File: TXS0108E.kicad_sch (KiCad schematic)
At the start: 1 part, among them U6 MAX98357A

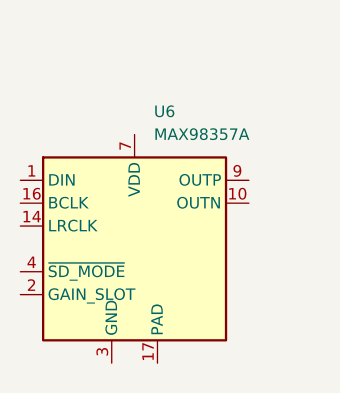
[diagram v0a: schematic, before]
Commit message: Add components: TXS0108E, FT232 oscillators/power/USB, symbol library table
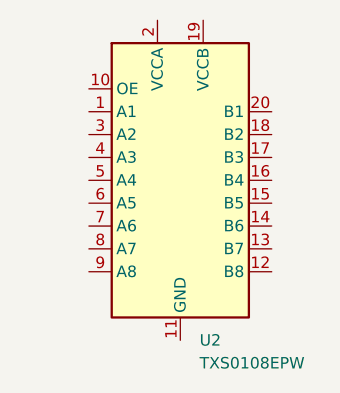
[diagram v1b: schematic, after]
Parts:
- removed U6: MAX98357A, Package_DFN_QFN:TQFN-16-1EP_3x3mm_P0.5mm_EP1.23x1.23mm, symbol Audio:MAX98357A
- added U2: TXS0108EPW, Package_SO:TSSOP-20_4.4x6.5mm_P0.65mm, symbol Logic_LevelTranslator:TXS0108EPW
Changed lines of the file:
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@@
 	(paper "A4")
 	(symbol
-		(lib_id "Audio:MAX98357A")
-		(at 144.78 99.06 0)
+		(lib_id "Logic_LevelTranslator:TXS0108EPW")
+		(at 149.86 91.44 0)
 		(unit 1)
 		(body_style 1)
@@
 		(dnp no)
 		(fields_autoplaced yes)
-		(property "Reference" "U6"
-			(at 146.9233 83.82 0)
+		(property "Reference" "U2"
+			(at 152.0033 109.22 0)
 			(show_name no)
 			(do_not_autoplace no)
@@
 			)
 		)
-		(property "Value" "MAX98357A"
-			(at 146.9233 86.36 0)
+		(property "Value" "TXS0108EPW"
+			(at 152.0033 111.76 0)
 			(show_name no)
 			(do_not_autoplace no)
@@
 			)
 		)
-		(property "Footprint" "Package_DFN_QFN:TQFN-16-1EP_3x3mm_P0.5mm_EP1.23x1.23mm"
-			(at 143.51 101.6 0)
+		(property "Footprint" "Package_SO:TSSOP-20_4.4x6.5mm_P0.65mm"
+			(at 149.86 110.49 0)
 			(hide yes)
 			(show_name no)
@@
 			)
 		)
-		(property "Datasheet" "https://www.analog.com/media/en/technical-documentation/data-sheets/MAX98357A-MAX98357B.pdf"
-			(at 144.78 101.6 0)
+		(property "Datasheet" "www.ti.com/lit/ds/symlink/txs0108e.pdf"
+			(at 149.86 93.98 0)
 			(hide yes)
 			(show_name no)
@@
 			)
 		)
-		(property "Description" "Mono DAC with amplifier, I2S, PCM, TDM, 32-bit, 96khz, 3.2W, TQFP-16"
-			(at 144.78 99.06 0)
+		(property "Description" "Bidirectional  level-shifting voltage translator, TSSOP-20"
+			(at 149.86 91.44 0)
 			(hide yes)
 			(show_name no)
@@
 			)
 		)
-		(pin "16"
+		(pin "19"
+		)
+		(pin "20"
+		)
+		(pin "14"
+		)
+		(pin "2"
+		)
+		(pin "5"
+		)
+		(pin "17"
+		)
+		(pin "7"
 		)
 		(pin "4"
 		)
-		(pin "5"
+		(pin "3"
 		)
-		(pin "15"
-		)
-		(pin "12"
-		)
-		(pin "13"
-		)
-		(pin "17"
-		)
-		(pin "2"
-		)
-		(pin "3"
+		(pin "18"
 		)
 		(pin "9"
 		)
-		(pin "1"
+		(pin "16"
 		)
 		(pin "10"
@@
 		(pin "11"
 		)
+		(pin "8"
+		)
+		(pin "12"
+		)
+		(pin "15"
+		)
+		(pin "13"
+		)
 		(pin "6"
 		)
-		(pin "7"
-		)
-		(pin "14"
-		)
-		(pin "8"
+		(pin "1"
 		)
 		(instances
 			(project "esp32_xiaozhi"
-				(path "/cae338e8-f342-43cb-b99a-a0486629133c/0b8c63fc-3109-4f1a-8140-b91a685f434f"
-					(reference "U6")
+				(path "/cae338e8-f342-43cb-b99a-a0486629133c/2567bb9e-06b8-4d2c-80a7-ee2453b67a65"
+					(reference "U2")
 					(unit 1)
 				)

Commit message: ESP32S3 branch initial changes
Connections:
- net A1: now reaches U2.1 (A1)
- net OE: now reaches U2.10 (OE)
- net GND: now reaches U2.11 (GND)
- net B8: now reaches U2.12 (B8)
- net B7: now reaches U2.13 (B7)
- net B6: now reaches U2.14 (B6)
- net B5: now reaches U2.15 (B5)
- net B4: now reaches U2.16 (B4)
- net B3: now reaches U2.17 (B3)
- net B2: now reaches U2.18 (B2)
- net +5V: now reaches U2.19 (VCCB)
- net +3V3: now reaches U2.2 (VCCA)
- net B1: now reaches U2.20 (B1)
- net A2: now reaches U2.3 (A2)
- net A3: now reaches U2.4 (A3)
- net A4: now reaches U2.5 (A4)
- net A5: now reaches U2.6 (A5)
- net A6: now reaches U2.7 (A6)
- net A7: now reaches U2.8 (A7)
- net A8: now reaches U2.9 (A8)

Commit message: Update KiCad project files
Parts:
- added C36, C37, C38: 100nf, Capacitor_SMD:C_0805_2012Metric, symbol Device:C
- added J11: Conn_01x08_Pin, symbol Connector:Conn_01x08_Pin
- added JP5, JP6: NL, Jumper:SolderJumper-2_P1.3mm_Open_RoundedPad1.0x1.5mm, symbol Jumper:Jumper_2_Open
- added Q10, Q11: FDN306P, Package_TO_SOT_SMD:SOT-23W, symbol FDN306P:FDN306P
- added Q7, Q8: Q_NPN_BCE, Package_TO_SOT_SMD:SOT-23W, symbol Device:Q_NPN_BCE
- added Q9: 2N7002, Package_TO_SOT_SMD:SOT-23, symbol Transistor_FET:2N7002
- added R49, R50, R51, R52, R53: 10k, Resistor_SMD:R_0603_1608Metric, symbol Device:R
- renumbered U2 to U7
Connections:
- net +3V3: now also C36.1, C37.1, JP5.2 (B), R50.2, R52.2
- net +5V: now also C38.1, JP6.2 (B)
- net B1: now also J11.1 (Pin_1)
- net B2: now also J11.2 (Pin_2)
- net B3: now also J11.3 (Pin_3)
- net B4: now also J11.4 (Pin_4)
- net B5: now also J11.5 (Pin_5)
- net B6: now also J11.6 (Pin_6)
- net B7: now also J11.7 (Pin_7)
- net B8: now also J11.8 (Pin_8)
- net GND: now also C36.2, C37.2, C38.2, Q7.3 (E), Q8.3 (E), Q9.2 (S), R53.1
- net OE: now also Q11.1, Q9.1 (G), R49.1, R53.2; no longer U7.10 (OE)
- new net: Q10.1, Q11.2, Q9.3 (D)
- new net: Q7.2 (C), R50.1, R51.1
- new net: Q8.1 (B), R51.2
- new net: JP5.1 (A), JP6.1 (A), Q10.3, Q11.3
- new net: Q7.1 (B), R49.2
- new net OEN: Q8.2 (C), R52.1, U7.10 (OE)
- new net vcc: Q10.2

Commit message: Remove unused schematic files, lock files, and backup directories
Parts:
- removed J11: Conn_01x08_Pin, symbol Connector:Conn_01x08_Pin
- added J11: logic_convert, Connector_PinHeader_1.27mm:PinHeader_1x09_P1.27mm_Vertical, symbol Connector:Conn_01x09_Pin
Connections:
- net B1: now also J11.1 (Pin_1)
- net B2: now also J11.2 (Pin_2)
- net B3: now also J11.3 (Pin_3)
- net B4: now also J11.4 (Pin_4)
- net B5: now also J11.5 (Pin_5)
- net B6: now also J11.6 (Pin_6)
- net B7: now also J11.7 (Pin_7)
- net B8: now also J11.8 (Pin_8)
- net GND: now also J11.9 (Pin_9)
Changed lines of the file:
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@@
+	(symbol
+		(lib_id "power:GND")
+		(at 191.77 104.14 0)
+		(unit 1)
+		(body_style 1)
+		(exclude_from_sim no)
+		(in_bom yes)
+		(on_board yes)
+		(in_pos_files yes)
+		(dnp no)
+		(property "Reference" "#PWR0111"
+			(at 191.77 110.49 0)
+			(hide yes)
+			(show_name no)
+			(do_not_autoplace no)
+			(effects
+				(font
+					(size 1.27 1.27)
+				)
+			)
+		)
+		(property "Value" "GND"
+			(at 190.246 107.188 0)
+			(show_name no)
+			(do_not_autoplace no)
+			(effects
+				(font
+					(size 1.27 1.27)
+				)
+			)
+		)
+		(property "Footprint" ""
+			(at 191.77 104.14 0)
+			(hide yes)
+			(show_name no)
+			(do_not_autoplace no)
+			(effects
+				(font
+					(size 1.27 1.27)
+				)
+			)
+		)
+		(property "Datasheet" ""
+			(at 191.77 104.14 0)
+			(hide yes)
+			(show_name no)
+			(do_not_autoplace no)
+			(effects
+				(font
+					(size 1.27 1.27)
+				)
+			)
+		)
+		(property "Description" "Power symbol creates a global label with name \"GND\" , ground"
+			(at 191.77 104.14 0)
+			(hide yes)
+			(show_name no)
+			(do_not_autoplace no)
+			(effects
+				(font
+					(size 1.27 1.27)
+				)
+			)
+		)
+		(pin "1"
+		)
+		(instances
+			(project "esp32_xiaozhi"
+				(path "/cae338e8-f342-43cb-b99a-a0486629133c/2567bb9e-06b8-4d2c-80a7-ee2453b67a65"
+					(reference "#PWR0111")
+					(unit 1)
+				)
+			)
+		)
+	)
 	(symbol
 		(lib_id "power:GND")
@@
 	)
 	(symbol
-		(lib_id "Connector:Conn_01x08_Pin")
-		(at 196.85 91.44 0)
-		(mirror y)
-		(unit 1)
-		(body_style 1)
-		(exclude_from_sim no)
-		(in_bom yes)
-		(on_board yes)
-		(in_pos_files yes)
-		(dnp no)
-		(fields_autoplaced yes)
-		(property "Reference" "J11"
-			(at 198.12 91.4399 0)
-			(show_name no)
-			(do_not_autoplace no)
-			(effects
-				(font
-					(size 1.27 1.27)
-				)
-				(justify right)
-			)
-		)
-		(property "Value" "Conn_01x08_Pin"
-			(at 198.12 93.9799 0)
-			(show_name no)
-			(do_not_autoplace no)
-			(effects
-				(font
-					(size 1.27 1.27)
-				)
-				(justify right)
-			)
-		)
-		(property "Footprint" ""
-			(at 196.85 91.44 0)
-			(hide yes)
-			(show_name no)
-			(do_not_autoplace no)
-			(effects
-				(font
-					(size 1.27 1.27)
-				)
-			)
-		)
-		(property "Datasheet" ""
-			(at 196.85 91.44 0)
-			(hide yes)
-			(show_name no)
-			(do_not_autoplace no)
-			(effects
-				(font
-					(size 1.27 1.27)
-				)
-			)
-		)
-		(property "Description" "Generic connector, single row, 01x08, script generated"
-			(at 196.85 91.44 0)
-			(hide yes)
-			(show_name no)
-			(do_not_autoplace no)
-			(effects
-				(font
-					(size 1.27 1.27)
-				)
-			)
-		)
-		(pin "3"
-		)
-		(pin "6"
-		)
-		(pin "2"
-		)
-		(pin "5"
-		)
-		(pin "1"
-		)
-		(pin "4"
-		)
-		(pin "7"
-		)
-		(pin "8"
-		)
-		(instances
-			(project "esp32_xiaozhi"
-				(path "/cae338e8-f342-43cb-b99a-a0486629133c/2567bb9e-06b8-4d2c-80a7-ee2453b67a65"
-					(reference "J11")
-					(unit 1)
-				)
-			)
-		)
-	)
-	(symbol
 		(lib_id "power:+3V3")
 		(at 53.34 52.07 0)
@@
 					(unit 1)
 				)
+			)
+		)
+	)
+	(symbol
+		(lib_id "Connector:Conn_01x09_Pin")
+		(at 196.85 93.98 0)
+		(mirror y)
+		(unit 1)
+		(body_style 1)
+		(exclude_from_sim no)
+		(in_bom yes)
+		(on_board yes)
+		(in_pos_files yes)
+		(dnp no)
+		(property "Reference" "J11"
+			(at 196.215 78.74 0)
+			(show_name no)
+			(do_not_autoplace no)
+			(effects
+				(font
+					(size 1.27 1.27)
+				)
+			)
+		)
+		(property "Value" "logic_convert"
+			(at 196.215 81.28 0)
+			(show_name no)
+			(do_not_autoplace no)
+			(effects
+				(font
+					(size 1.27 1.27)
+				)
+			)
+		)
+		(property "Footprint" "Connector_PinHeader_1.27mm:PinHeader_1x09_P1.27mm_Vertical"
+			(at 202.438 110.236 0)
+			(show_name no)
+			(do_not_autoplace no)
+			(effects
+				(font
+					(size 1.27 1.27)
+				)
+			)
+		)
+		(property "Datasheet" ""
+			(at 196.85 93.98 0)
+			(hide yes)
+			(show_name no)
+			(do_not_autoplace no)
+			(effects
+				(font
+					(size 1.27 1.27)
+				)
+			)
+		)
+		(property "Description" "Generic connector, single row, 01x09, script generated"
+			(at 196.85 93.98 0)
+			(hide yes)
+			(show_name no)
+			(do_not_autoplace no)
+			(effects
+				(font
+					(size 1.27 1.27)
+				)
+			)
+		)
+		(pin "8"
+		)
+		(pin "5"
+		)
+		(pin "4"
+		)
+		(pin "1"
+		)
+		(pin "2"
+		)
+		(pin "3"
+		)
+		(pin "7"
+		)
+		(pin "9"
+		)
+		(pin "6"
+		)
+		(instances
+			(project "esp32_xiaozhi"
+				(path "/cae338e8-f342-43cb-b99a-a0486629133c/2567bb9e-06b8-4d2c-80a7-ee2453b67a65"
+					(reference "J11")
+					(unit 1)
+				)

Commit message: Update all schematic files and project
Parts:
- J11: footprint Connector_PinHeader_1.27mm:PinHeader_1x09_P1.27mm_Vertical -> Connector_PinHeader_2.54mm:PinHeader_2x05_P2.54mm_Vertical
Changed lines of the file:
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@@
 			)
 		)
-		(property "Footprint" "Connector_PinHeader_1.27mm:PinHeader_1x09_P1.27mm_Vertical"
+		(property "Footprint" "Connector_PinHeader_2.54mm:PinHeader_2x05_P2.54mm_Vertical"
 			(at 202.438 110.236 0)
 			(show_name no)

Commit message: Actualización de esquema y PCB del proyecto ESP32C6 Xiaozhi
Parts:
- added C55, C56: 100nf, Capacitor_SMD:C_0805_2012Metric, symbol Device:C
- added D5: LED, Diode_SMD:D_0805_2012Metric, symbol Device:LED
- added J23: TP_VCC, TestPoint:TestPoint_THTPad_1.0x1.0mm_Drill0.5mm, symbol Connector:Conn_01x01_Pin
- added R29: 2k2, Resistor_SMD:R_0805_2012Metric, symbol Device:R
- added R68: 10k, Resistor_SMD:R_0603_1608Metric, symbol Device:R
- R50, R51, R52: value 10k -> 4k7
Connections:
- net +3V3: no longer R50.2, R52.2
- net +5V: now also R50.2, R52.2
- net A8: now also R68.2
- net GND: now also C55.2, C56.2, R29.1
- net OE: no longer Q11.1, Q9.1 (G), R53.2
- net vcc: now also C55.1, D5.2 (A), J23.1 (Pin_1)
- net at JP5.1 (A), JP6.1 (A), Q10.3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: now also C56.1
- new net: D5.1 (K), R29.2
- new net CONTROL: Q11.1, Q9.1 (G), R53.2, R68.1

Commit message: Actualizaciones para versión single ESP32C6
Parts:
- removed J11: logic_convert, Connector_PinHeader_2.54mm:PinHeader_2x05_P2.54mm_Vertical, symbol Connector:Conn_01x09_Pin
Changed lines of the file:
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@@
+		)
+	)
+	(hierarchical_label "B5"
+		(shape input)
+		(at 191.77 93.98 0)
+		(effects
+			(font
+				(size 1.27 1.27)
+			)
+			(justify left)
+		)
+	)
+	(hierarchical_label "B6"
+		(shape input)
+		(at 191.77 96.52 0)
+		(effects
+			(font
+				(size 1.27 1.27)
+			)
+			(justify left)
+		)
+	)
+	(hierarchical_label "B7"
+		(shape input)
+		(at 191.77 99.06 0)
+		(effects
+			(font
+				(size 1.27 1.27)
+			)
+			(justify left)
 		)
 	)
@@
 		)
 	)
+	(hierarchical_label "B4"
+		(shape input)
+		(at 191.77 91.44 0)
+		(effects
+			(font
+				(size 1.27 1.27)
+			)
+			(justify left)
+		)
+	)
 	(hierarchical_label "A1"
 		(shape input)
@@
 		)
 	)
+	(hierarchical_label "B8"
+		(shape input)
+		(at 191.77 101.6 0)
+		(effects
+			(font
+				(size 1.27 1.27)
+			)
+			(justify left)
+		)
+	)
+	(hierarchical_label "B1"
+		(shape input)
+		(at 191.77 83.82 0)
+		(effects
+			(font
+				(size 1.27 1.27)
+			)
+			(justify left)
+		)
+	)
+	(hierarchical_label "B3"
+		(shape input)
+		(at 191.77 88.9 0)
+		(effects
+			(font
+				(size 1.27 1.27)
+			)
+			(justify left)
+		)
+	)
+	(hierarchical_label "B2"
+		(shape input)
+		(at 191.77 86.36 0)
+		(effects
+			(font
+				(size 1.27 1.27)
+			)
+			(justify left)
+		)
+	)
 	(hierarchical_label "A4"
 		(shape input)
@@
 	(symbol
 		(lib_id "power:GND")
-		(at 191.77 104.14 0)
-		(unit 1)
-		(body_style 1)
-		(exclude_from_sim no)
-		(in_bom yes)
-		(on_board yes)
-		(in_pos_files yes)
-		(dnp no)
-		(property "Reference" "#PWR0111"
-			(at 191.77 110.49 0)
-			(hide yes)
-			(show_name no)
-			(do_not_autoplace no)
-			(effects
-				(font
-					(size 1.27 1.27)
-				)
-			)
-		)
-		(property "Value" "GND"
-			(at 190.246 107.188 0)
-			(show_name no)
-			(do_not_autoplace no)
-			(effects
-				(font
-					(size 1.27 1.27)
-				)
-			)
-		)
-		(property "Footprint" ""
-			(at 191.77 104.14 0)
-			(hide yes)
-			(show_name no)
-			(do_not_autoplace no)
-			(effects
-				(font
-					(size 1.27 1.27)
-				)
-			)
-		)
-		(property "Datasheet" ""
-			(at 191.77 104.14 0)
-			(hide yes)
-			(show_name no)
-			(do_not_autoplace no)
-			(effects
-				(font
-					(size 1.27 1.27)
-				)
-			)
-		)
-		(property "Description" "Power symbol creates a global label with name \"GND\" , ground"
-			(at 191.77 104.14 0)
-			(hide yes)
-			(show_name no)
-			(do_not_autoplace no)
-			(effects
-				(font
-					(size 1.27 1.27)
-				)
-			)
-		)
-		(pin "1"
-		)
-		(instances
-			(project "esp32_xiaozhi"
-				(path "/cae338e8-f342-43cb-b99a-a0486629133c/2567bb9e-06b8-4d2c-80a7-ee2453b67a65"
-					(reference "#PWR0111")
-					(unit 1)
-				)
-			)
-		)
-	)
-	(symbol
-		(lib_id "power:GND")
 		(at 34.29 69.85 0)
 		(unit 1)
@@
 					(unit 1)
 				)
-			)
-		)
-	)
-	(symbol
-		(lib_id "Connector:Conn_01x09_Pin")
-		(at 196.85 93.98 0)
-		(mirror y)
-		(unit 1)
-		(body_style 1)
-		(exclude_from_sim no)
-		(in_bom yes)
-		(on_board yes)
-		(in_pos_files yes)
-		(dnp no)
-		(property "Reference" "J11"
-			(at 196.215 78.74 0)
-			(show_name no)
-			(do_not_autoplace no)
-			(effects
-				(font
-					(size 1.27 1.27)
-				)
-			)
-		)
-		(property "Value" "logic_convert"
-			(at 196.215 81.28 0)
-			(show_name no)
-			(do_not_autoplace no)
-			(effects
-				(font
-					(size 1.27 1.27)
-				)
-			)
-		)
-		(property "Footprint" "Connector_PinHeader_2.54mm:PinHeader_2x05_P2.54mm_Vertical"
-			(at 202.438 110.236 0)
-			(show_name no)
-			(do_not_autoplace no)
-			(effects
-				(font
-					(size 1.27 1.27)
-				)
-			)
-		)
-		(property "Datasheet" ""
-			(at 196.85 93.98 0)
-			(hide yes)
-			(show_name no)
-			(do_not_autoplace no)
-			(effects
-				(font
-					(size 1.27 1.27)
-				)
-			)
-		)
-		(property "Description" "Generic connector, single row, 01x09, script generated"
-			(at 196.85 93.98 0)
-			(hide yes)
-			(show_name no)
-			(do_not_autoplace no)
-			(effects
-				(font
-					(size 1.27 1.27)
-				)
-			)
-		)
-		(pin "8"
-		)
-		(pin "5"
-		)
-		(pin "4"
-		)
-		(pin "1"
-		)
-		(pin "2"
-		)
-		(pin "3"
-		)
-		(pin "7"
-		)
-		(pin "9"
-		)
-		(pin "6"
-		)
-		(instances
-			(project "esp32_xiaozhi"
-				(path "/cae338e8-f342-43cb-b99a-a0486629133c/2567bb9e-06b8-4d2c-80a7-ee2453b67a65"
-					(reference "J11")
-					(unit 1)
-				)

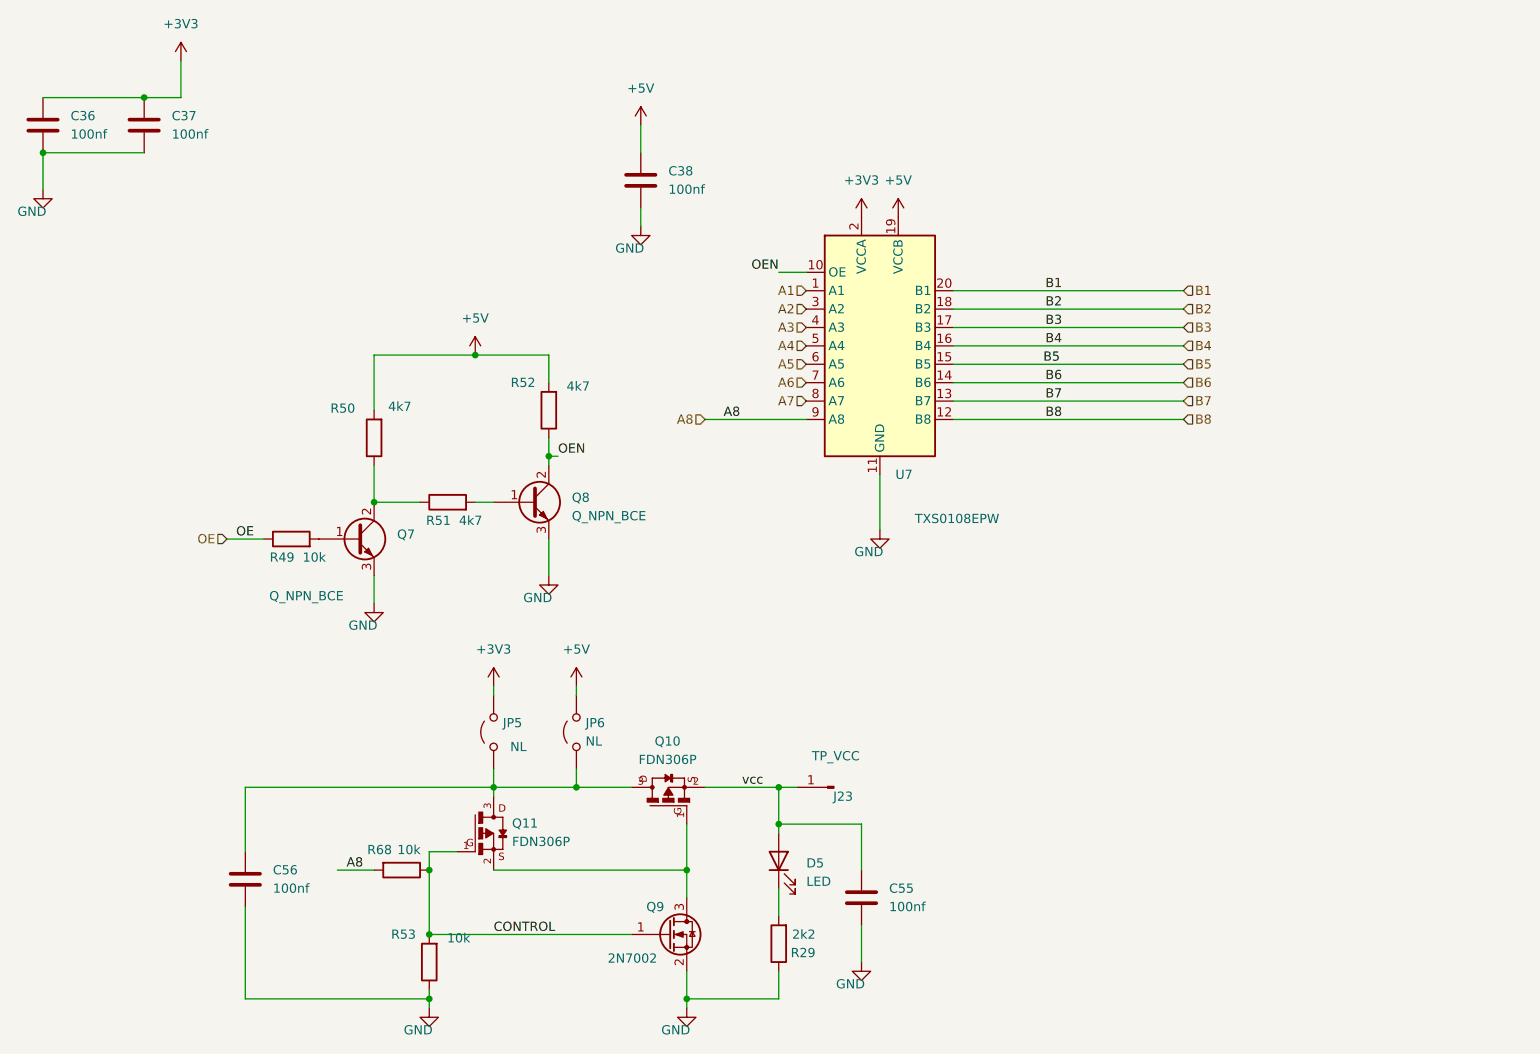
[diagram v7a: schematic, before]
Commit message: SCH: Update TXS0108E level shifter schematic
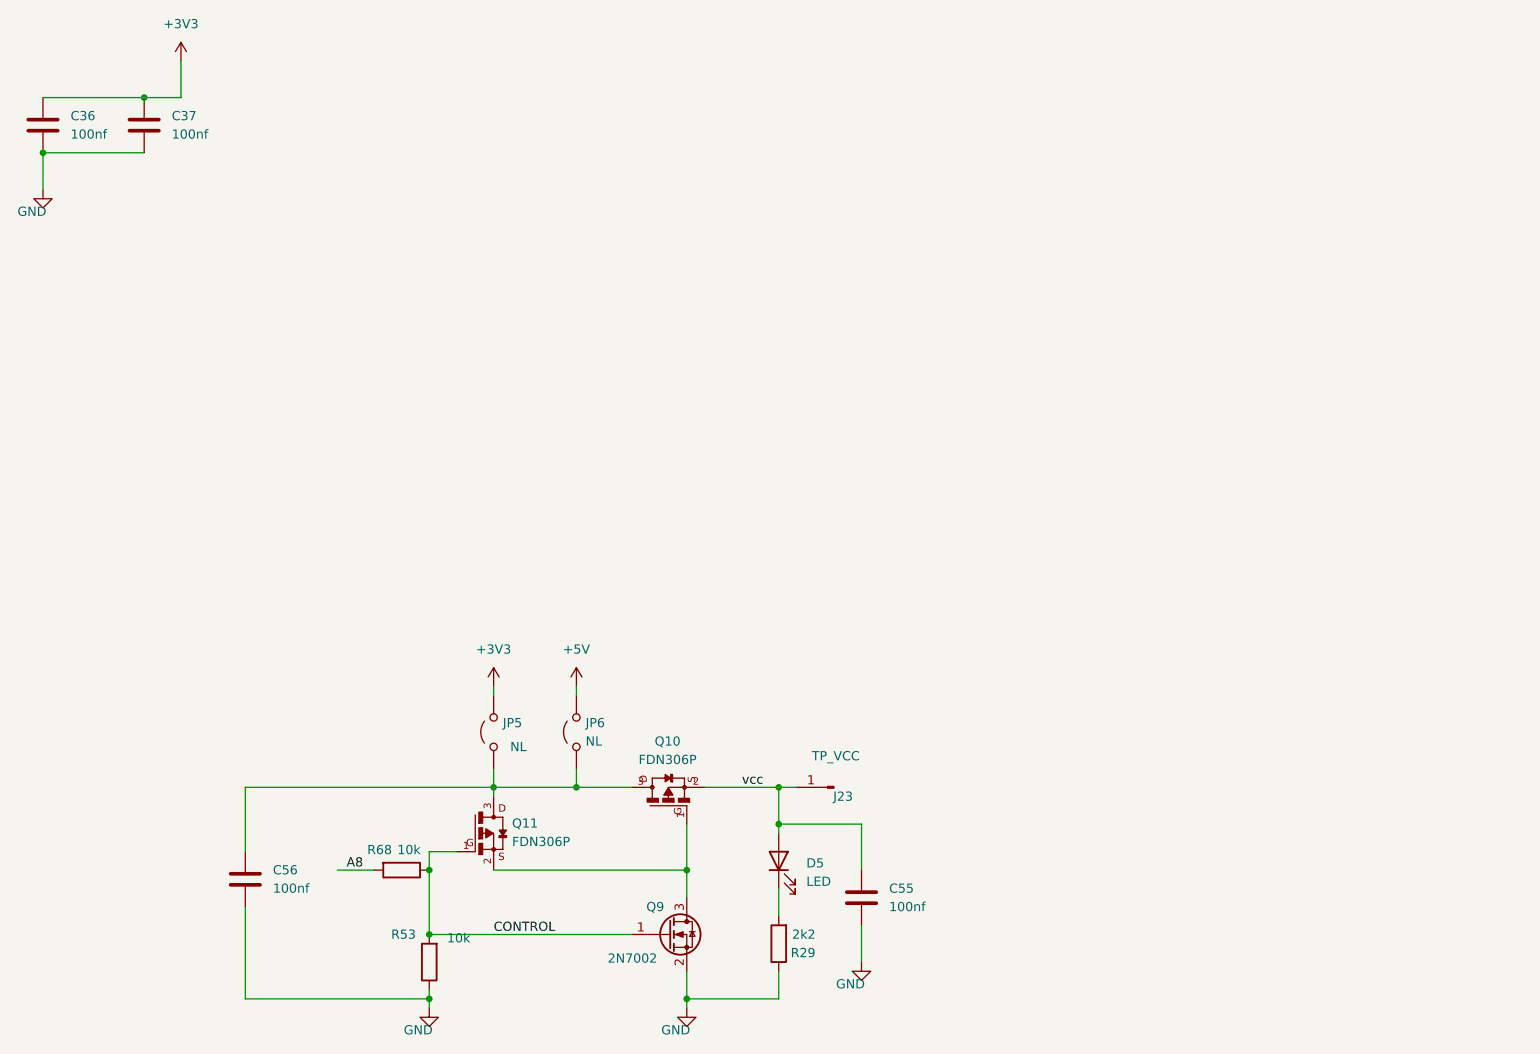
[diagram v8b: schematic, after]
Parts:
- removed C38: 100nf, Capacitor_SMD:C_0805_2012Metric, symbol Device:C
- removed Q7, Q8: Q_NPN_BCE, Package_TO_SOT_SMD:SOT-23W, symbol Device:Q_NPN_BCE
- removed R49: 10k, Resistor_SMD:R_0603_1608Metric, symbol Device:R
- removed R50, R51, R52: 4k7, Resistor_SMD:R_0603_1608Metric, symbol Device:R
- removed U7: TXS0108EPW, Package_SO:TSSOP-20_4.4x6.5mm_P0.65mm, symbol Logic_LevelTranslator:TXS0108EPW
